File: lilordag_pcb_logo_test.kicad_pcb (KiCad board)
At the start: 2 copper layers, 98.1 x 100 mm, 175 parts, among them J1 USB4105-GF-A, J2 826629-7, J3 826629-7, Q1 BC846, Q2 BC846, Q3 MMBT3906, Q4 MMBT3906, Q5 BC846, Q6 BC846, Q7 SSM3J56MFV, Q8 SSM3J56MFV, SW1 PCM12SMTR, SW2 PCM12SMTR, SW3 SW_MEC_5G, SW4 PCM12SMTR, SW5 SW_MEC_5G, SW6 SW_MEC_5G, SW7 SW_MEC_5G, U1 ESP32-C3-MINI-1-N4, U2 WS2812B-B, U3 WS2812B-B, U4 WS2812B-B, U5 WS2812B-B

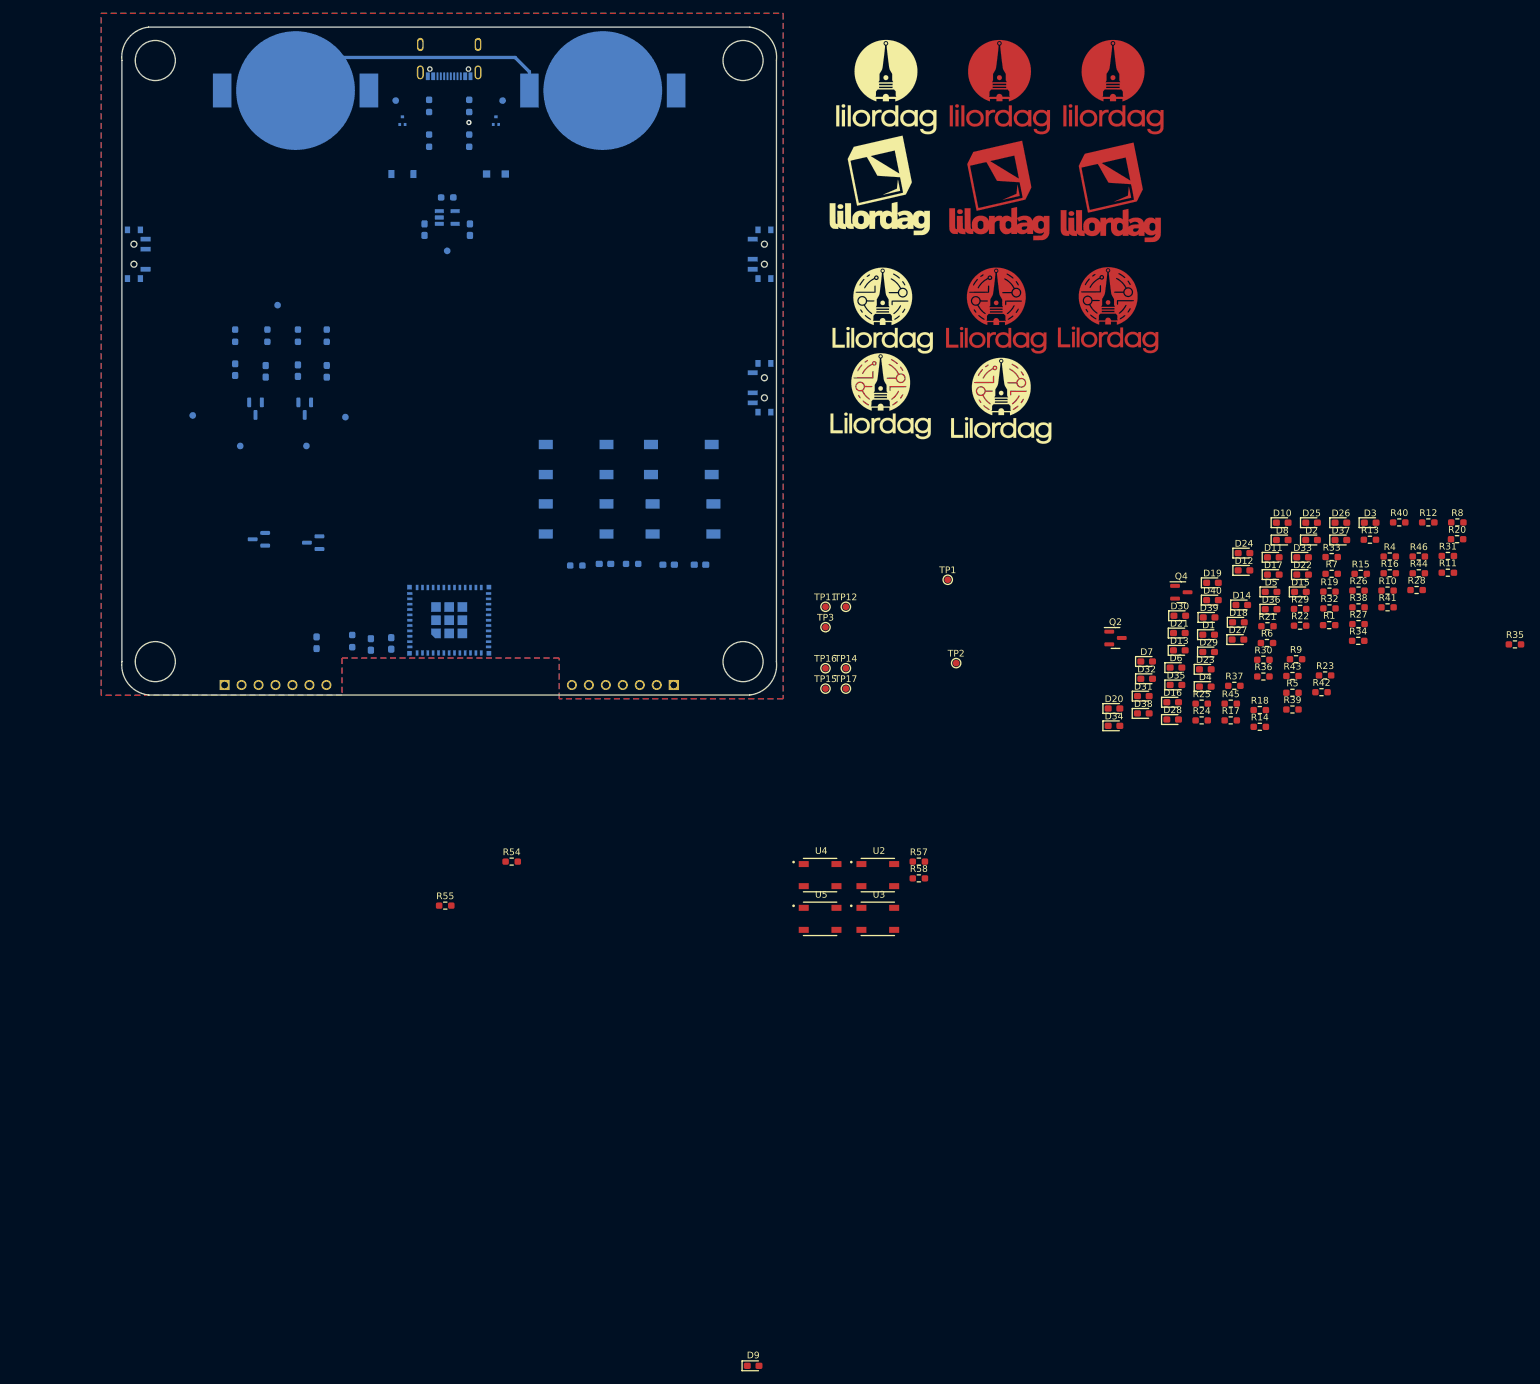
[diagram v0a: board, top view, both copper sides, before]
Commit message: All the elements are on the board
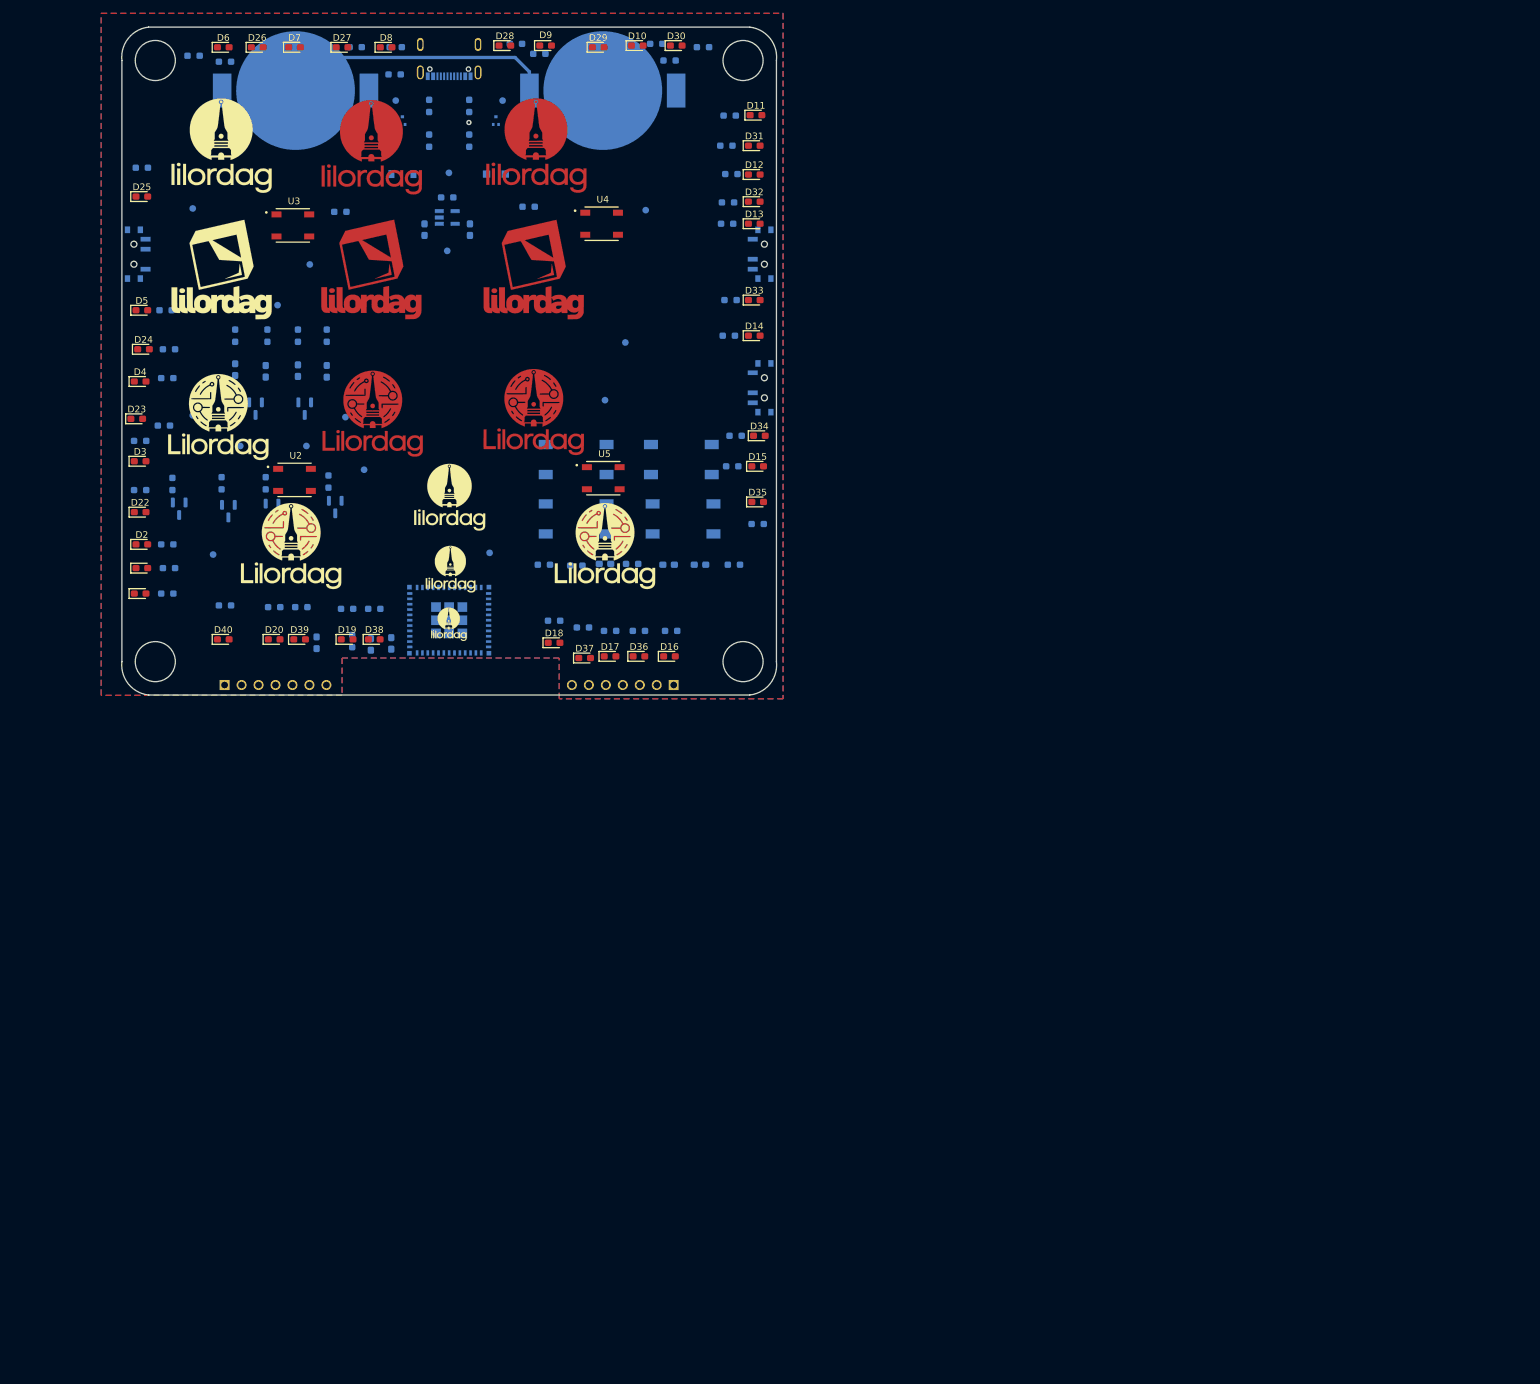
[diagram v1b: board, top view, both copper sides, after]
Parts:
- added Ref**: Val**, pcb_logos:simple_tower_5x5, F.Cu at (77.0, 119.4)
- added Ref**: Val**, pcb_logos:drawing, F.Cu at (77.0, 99.8)
- added Ref**: Val**, pcb_logos:simple_tower_7x7, F.Cu at (77.2, 111.3)
- Q2, Q4, R1, R10, R11, R12, R13, R14, R15, R16, R17, R18, R19, R20, R21, R22, R23, R24, R25, R26, R27, R28, R29, R30, R31, R32, R33, R34, R35, R36, R37, R38, R39, R4, R40, R41, R42, R43, R44, R45, R46, R5, R54, R55, R57, R58, R6, R7, R8, R9, TP1, TP11, TP12, TP14, TP15, TP16, TP17, TP2, TP3: moved to B.Cu
- moved R8 201.7 mm to (38.7, 34.3), turned to 180 degrees
- moved D9 200.1 mm to (91.4, 32.8)
- moved R28 190.2 mm to (35.1, 78.2), turned to 180 degrees
- moved R12 188.1 mm to (35.6, 98.4), turned to -90 degrees
- moved R29 185.6 mm to (31.0, 51.1), turned to 180 degrees
- moved D3 184.4 mm to (30.7, 95.0)
- moved R4 183.0 mm to (34.8, 107.4), turned to 180 degrees
- moved R26 183.0 mm to (30.7, 99.3), turned to 180 degrees
- moved D25 181.8 mm to (31.0, 55.4)
- moved R27 181.3 mm to (34.3, 89.7), turned to 180 degrees
- moved R30 179.4 mm to (43.4, 35.2), turned to 180 degrees
- moved R7 179.0 mm to (34.5, 72.4), turned to 180 degrees
- moved R46 178.9 mm to (43.4, 116.6), turned to 180 degrees
- moved R31 177.3 mm to (49.5, 98.3), turned to -90 degrees
- moved D26 177.2 mm to (48.3, 33.0)
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
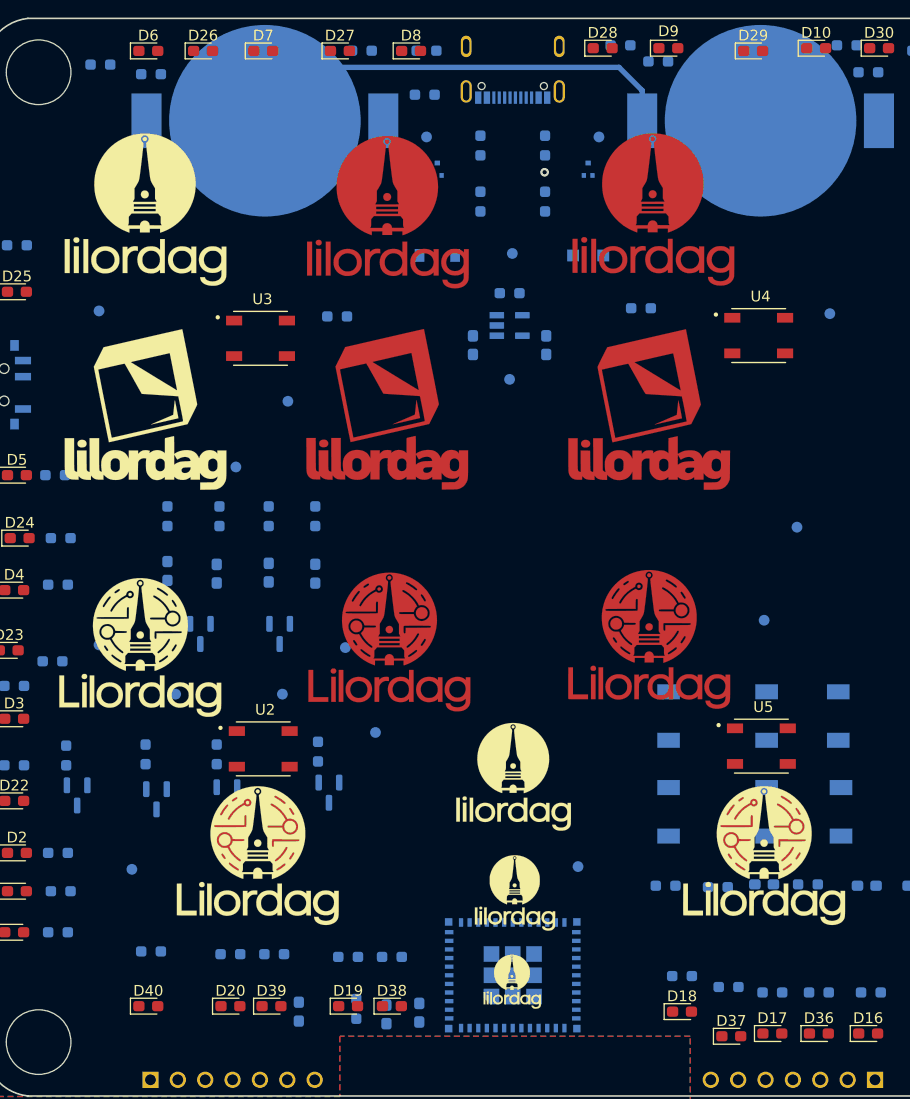
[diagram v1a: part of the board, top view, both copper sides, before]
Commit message: outter logos locked
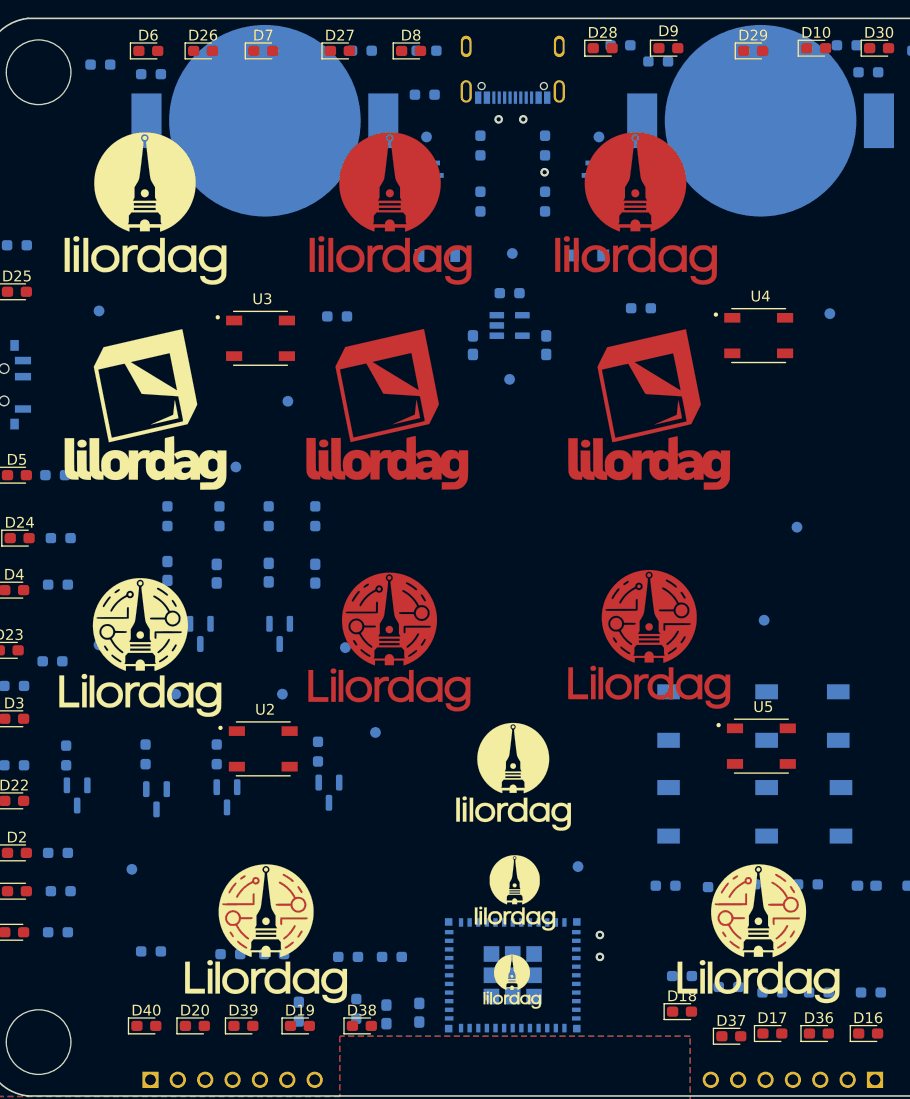
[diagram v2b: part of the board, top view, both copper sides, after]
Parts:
- moved Ref** 7.29 mm to (55.1, 114.0)
- moved Ref** 7.27 mm to (100.8, 114.0)
- moved D19 4.83 mm to (57.2, 123.5)
- moved D20 3.78 mm to (47.5, 123.5)
- moved D38 3.34 mm to (63.0, 123.5)
- moved D39 3.19 mm to (52.0, 123.5)
- moved D40 1.84 mm to (43.0, 123.5)
- moved Ref** 1.61 mm to (93.6, 53.0)
- moved Ref** 0.58 mm to (116.4, 53.0)
- moved Ref** 0.42 mm to (70.9, 53.0)
- moved Ref** 0.10 mm to (48.1, 53.0)
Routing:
- net Net-(BT1-Pad3): track 38.8 -> 0.00 mm
- net USB_D-: vias 0 -> 2
- net USB_D+: vias 0 -> 2
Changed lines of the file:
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@@
       (net 83 "Net-(TP16-Pad1)") (pinfunction "DIN") (pintype "input"))
   )
-  (footprint "pcb_logos:tower-complex-golden-stars" (layer "F.Cu")
-    (at 101.322962 106.750281)
+  (footprint "pcb_logos:tower-complex-golden-stars" locked (layer "F.Cu")
+    (at 100.8 114)
     (attr through_hole)
     (fp_text reference "Ref**" (at 0 0) (layer "F.SilkS") hide
@@
   )
   (footprint "LED_SMD:LED_0603_1608Metric_Pad1.05x0.95mm_HandSolder" (layer "F.Cu")
-    (at 43.18 121.666)
+    (at 43 123.5)
     (descr "LED SMD 0603 (1608 Metric), square (rectangular) end terminal, IPC_7351 nominal, (Body size source: http://www.tortai-tech.com/upload/download/2011102023233369053.pdf), generated with kicad-footprint-generator")
     (tags "LED handsolder")
@@
   )
   (footprint "LED_SMD:LED_0603_1608Metric_Pad1.05x0.95mm_HandSolder" (layer "F.Cu")
-    (at 50.8 121.666)
+    (at 47.5 123.5)
     (descr "LED SMD 0603 (1608 Metric), square (rectangular) end terminal, IPC_7351 nominal, (Body size source: http://www.tortai-tech.com/upload/download/2011102023233369053.pdf), generated with kicad-footprint-generator")
     (tags "LED handsolder")
@@
     )
   )
-  (footprint "pcb_logos:logo-tower-simple-light-green" (layer "F.Cu")
-    (at 70.612 53.34)
+  (footprint "pcb_logos:logo-tower-simple-light-green" locked (layer "F.Cu")
+    (at 70.86 53)
     (attr through_hole)
     (fp_text reference "Ref**" (at 0 0) (layer "F.SilkS") hide
@@
   )
   (footprint "LED_SMD:LED_0603_1608Metric_Pad1.05x0.95mm_HandSolder" (layer "F.Cu")
-    (at 54.61 121.666)
+    (at 52 123.5)
     (descr "LED SMD 0603 (1608 Metric), square (rectangular) end terminal, IPC_7351 nominal, (Body size source: http://www.tortai-tech.com/upload/download/2011102023233369053.pdf), generated with kicad-footprint-generator")
     (tags "LED handsolder")
@@
   )
   (footprint "pcb_logos:logo-tower-simple-gold" (layer "F.Cu")
-    (at 95.25 53.086)
+    (at 93.64 53)
     (attr through_hole)
     (fp_text reference "Ref**" (at 0 0) (layer "F.SilkS") hide
@@
   )
   (footprint "LED_SMD:LED_0603_1608Metric_Pad1.05x0.95mm_HandSolder" (layer "F.Cu")
-    (at 61.722 121.666)
+    (at 57.25 123.5)
     (descr "LED SMD 0603 (1608 Metric), square (rectangular) end terminal, IPC_7351 nominal, (Body size source: http://www.tortai-tech.com/upload/download/2011102023233369053.pdf), generated with kicad-footprint-generator")
     (tags "LED handsolder")
@@
     )
   )
-  (footprint "pcb_logos:logo-tower-simple-white" (layer "F.Cu")
-    (at 48.122417 53.10307)
+  (footprint "pcb_logos:logo-tower-simple-white" locked (layer "F.Cu")
+    (at 48.122417 53)
     (attr through_hole)
     (fp_text reference "Ref**" (at 0 0) (layer "F.SilkS") hide
@@
   )
   (footprint "LED_SMD:LED_0603_1608Metric_Pad1.05x0.95mm_HandSolder" (layer "F.Cu")
-    (at 65.786 121.666)
+    (at 63 123.5)
     (descr "LED SMD 0603 (1608 Metric), square (rectangular) end terminal, IPC_7351 nominal, (Body size source: http://www.tortai-tech.com/upload/download/2011102023233369053.pdf), generated with kicad-footprint-generator")
     (tags "LED handsolder")
@@
     )
   )
-  (footprint "pcb_logos:tower-complex-light-green-stars" (layer "F.Cu")
-    (at 54.332962 106.750281)
+  (footprint "pcb_logos:tower-complex-light-green-stars" locked (layer "F.Cu")
+    (at 55.1 114)
     (attr through_hole)
     (fp_text reference "Ref**" (at 0 0) (layer "F.SilkS") hide
@@
       ) (layer "F.SilkS") (width 0.01) (fill solid))
   )
-  (footprint "pcb_logos:logo-tower-simple-clear" (layer "F.Cu")
-    (at 115.824 53.086)
+  (footprint "pcb_logos:logo-tower-simple-clear" locked (layer "F.Cu")
+    (at 116.4 53)
     (attr through_hole)
     (fp_text reference "Ref**" (at 0 0) (layer "F.SilkS") hide
@@
       (offset (xyz 0 0 4.3))
       (scale (xyz 1 1 1))
-      (rotate (xyz -90 0 0))
+      (rotate (xyz -90 0 180))
     )
   )
@@
   (gr_arc locked (start 122 30) (mid 125.035534 31.671573) (end 126 35) (layer "Edge.Cuts") (width 0.15))
   (via (at 79.955044 44.281218) (size 0.8) (drill 0.4) (layers "F.Cu" "B.Cu") (free) (net 0))
-  (segment (start 89.015 39.5) (end 89.015 36.691) (width 0.5) (layer "B.Cu") (net 65))
-  (segment (start 86.868 34.544) (end 60.956 34.544) (width 0.5) (layer "B.Cu") (net 65))
-  (segment (start 60.956 34.544) (end 56 39.5) (width 0.5) (layer "B.Cu") (net 65))
-  (segment (start 89.015 36.691) (end 86.868 34.544) (width 0.5) (layer "B.Cu") (net 65))
+  (via (at 85.09 115.062) (size 0.8) (drill 0.4) (layers "F.Cu" "B.Cu") (free) (net 54))
+  (via (at 75.692 39.37) (size 0.8) (drill 0.4) (layers "F.Cu" "B.Cu") (free) (net 54))
+  (via (at 77.978 39.37) (size 0.8) (drill 0.4) (layers "F.Cu" "B.Cu") (free) (net 55))
+  (via (at 85.09 117.094) (size 0.8) (drill 0.4) (layers "F.Cu" "B.Cu") (free) (net 55))
   (zone locked (net 15) (net_name "GND") (layers F&B.Cu) (hatch edge 0.508)
     (connect_pads (clearance 0.508))

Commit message: left lide logos locked
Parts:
- moved Ref** 0.27 mm to (43.5, 87.4)
- moved Ref** 0.25 mm to (49.5, 73.2)
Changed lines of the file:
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@@
   )
   (footprint "pcb_logos:candy-simple-white" (layer "F.Cu")
-    (at 49.201917 73.168839)
+    (at 49.45 73.168839)
     (attr through_hole)
     (fp_text reference "Ref**" (at 0 0) (layer "F.SilkS") hide
@@
   )
   (footprint "pcb_logos:tower-complex-white" (layer "F.Cu")
-    (at 43.18 87.376)
+    (at 43.45 87.376)
     (attr through_hole)
     (fp_text reference "Ref**" (at 0 0) (layer "F.SilkS") hide
